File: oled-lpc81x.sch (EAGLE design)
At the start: 14 parts, among them X1 PIIKKIRIMA-2X8, X2 PIIKKIRIMA-8

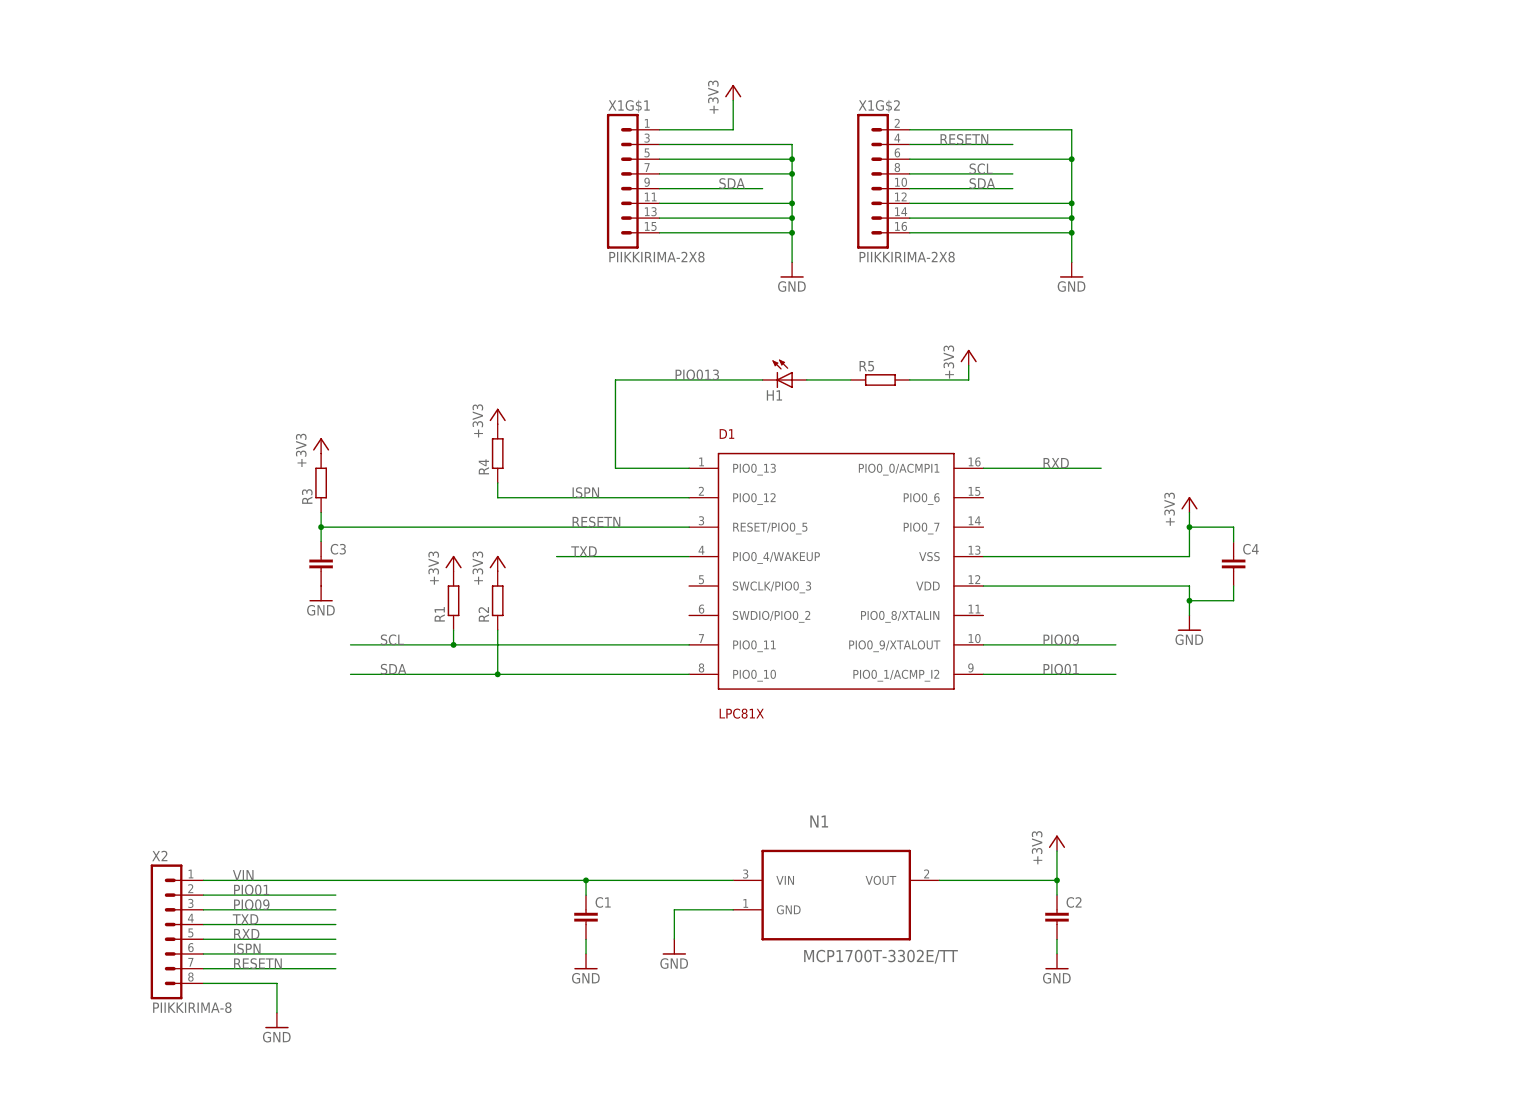
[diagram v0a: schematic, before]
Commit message: Changed busses
OLED now 3-wire SPI
I2C external to header
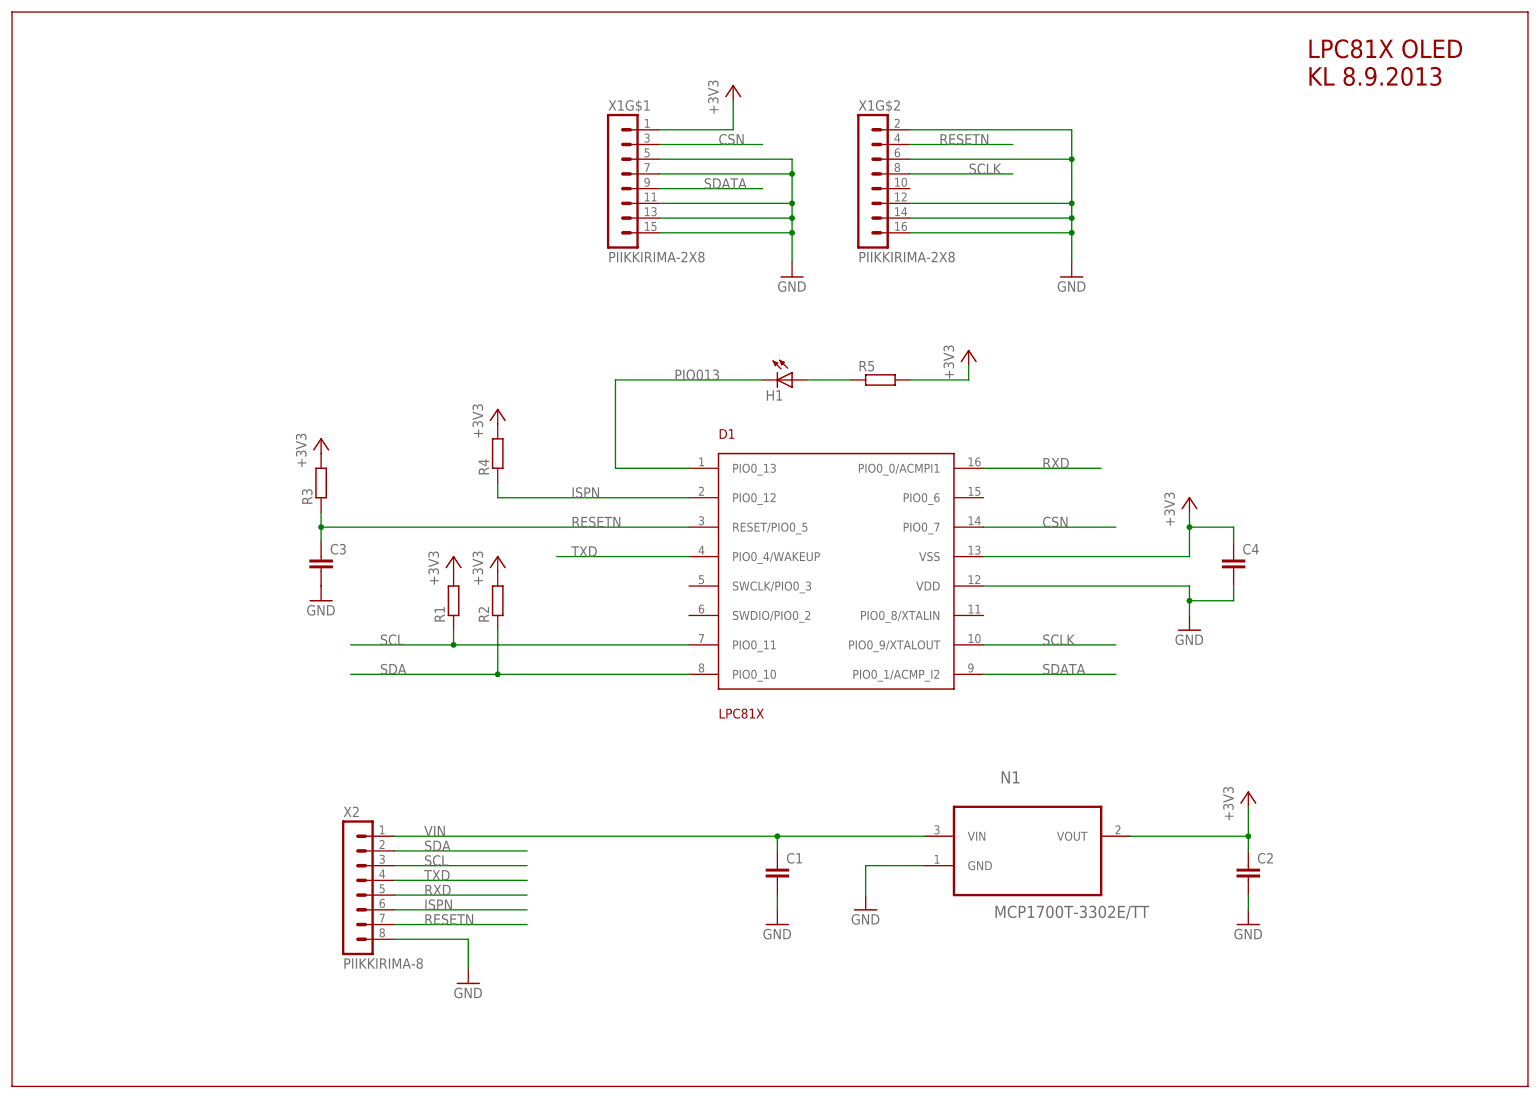
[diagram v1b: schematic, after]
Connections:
- removed net PIO01: D1.PIO0_1/ACMP_I2, X2.2
- removed net PIO09: D1.PIO0_9/XTALOUT, X2.3
- new net CSN: D1.PIO0_7, X1G$1.2
- new net SCLK: D1.PIO0_9/XTALOUT, X1G$2.4
- new net SDATA: D1.PIO0_1/ACMP_I2, X1G$1.5
- net GND: no longer X1G$1.2
- net SCL: now also X2.3; no longer X1G$2.4
- net SDA: now also X2.2; no longer X1G$2.5
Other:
- note added: "LPC81X OLED KL 8.9.2013"
- moved on the sheet: C1, C2, N1, X2

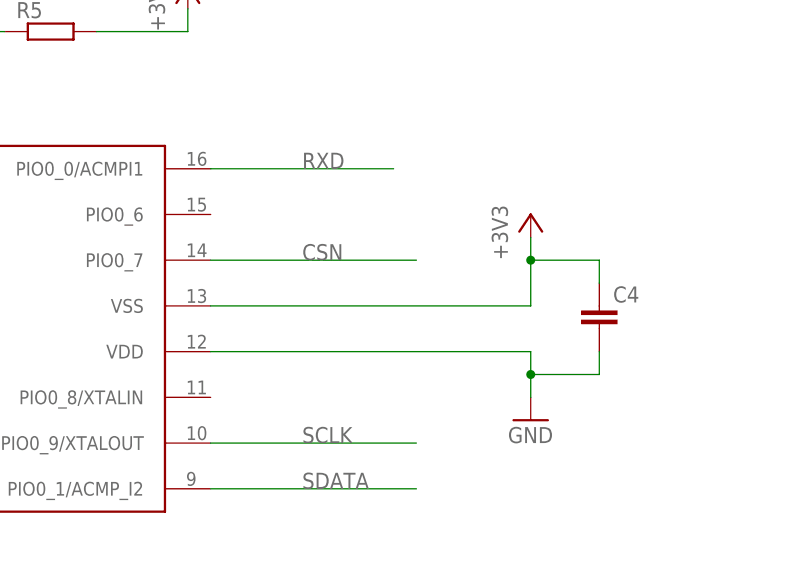
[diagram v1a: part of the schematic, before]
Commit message: v2 - VDD/VSS connection to LPC812 corrected.
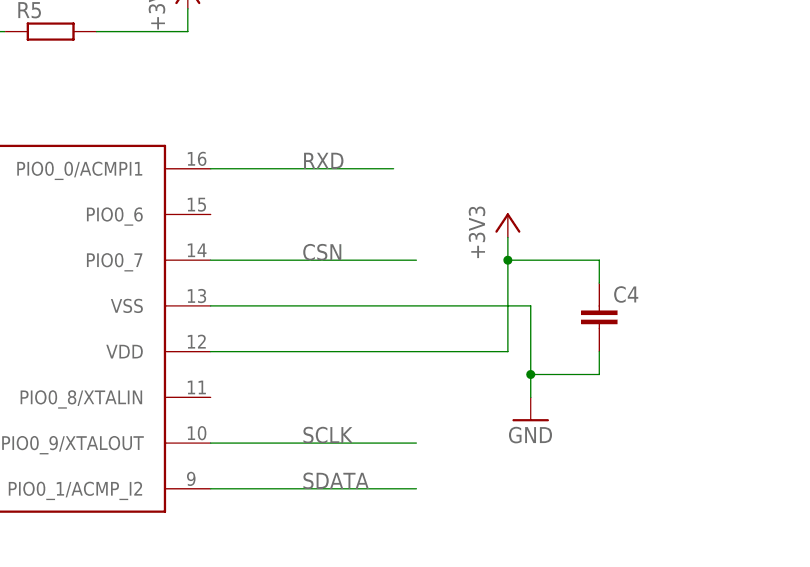
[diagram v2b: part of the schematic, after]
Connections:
- net +3V3: now also D1.VDD; no longer D1.VSS
- net GND: now also D1.VSS; no longer D1.VDD
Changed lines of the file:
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@@
 <instance part="GND5" gate="1" x="152.4" y="-76.2"/>
 <instance part="GND6" gate="1" x="142.24" y="-25.4"/>
-<instance part="+3V3" gate="G$1" x="142.24" y="-2.54"/>
+<instance part="+3V3" gate="G$1" x="139.7" y="-2.54"/>
 <instance part="C1" gate="G$1" x="71.12" y="-66.04"/>
 <instance part="C2" gate="G$1" x="152.4" y="-66.04"/>
@@
 </segment>
 <segment>
-<pinref part="D1" gate="G$1" pin="VSS"/>
-<wire x1="106.68" y1="-12.7" x2="142.24" y2="-12.7" width="0.1524" layer="91"/>
-<wire x1="142.24" y1="-12.7" x2="142.24" y2="-7.62" width="0.1524" layer="91"/>
 <pinref part="+3V3" gate="G$1" pin="+3V3"/>
 <pinref part="C4" gate="G$1" pin="1"/>
-<wire x1="142.24" y1="-7.62" x2="142.24" y2="-5.08" width="0.1524" layer="91"/>
-<wire x1="142.24" y1="-7.62" x2="149.86" y2="-7.62" width="0.1524" layer="91"/>
+<wire x1="139.7" y1="-7.62" x2="139.7" y2="-5.08" width="0.1524" layer="91"/>
+<wire x1="139.7" y1="-7.62" x2="149.86" y2="-7.62" width="0.1524" layer="91"/>
 <wire x1="149.86" y1="-7.62" x2="149.86" y2="-10.16" width="0.1524" layer="91"/>
-<junction x="142.24" y="-7.62"/>
+<junction x="139.7" y="-7.62"/>
+<pinref part="D1" gate="G$1" pin="VDD"/>
+<wire x1="106.68" y1="-17.78" x2="139.7" y2="-17.78" width="0.1524" layer="91"/>
+<wire x1="139.7" y1="-17.78" x2="139.7" y2="-7.62" width="0.1524" layer="91"/>
 </segment>
 <segment>
@@
 </segment>
 <segment>
-<pinref part="D1" gate="G$1" pin="VDD"/>
-<wire x1="106.68" y1="-17.78" x2="142.24" y2="-17.78" width="0.1524" layer="91"/>
-<wire x1="142.24" y1="-17.78" x2="142.24" y2="-20.32" width="0.1524" layer="91"/>
 <pinref part="GND6" gate="1" pin="GND"/>
 <pinref part="C4" gate="G$1" pin="2"/>
@@
 <wire x1="142.24" y1="-20.32" x2="149.86" y2="-20.32" width="0.1524" layer="91"/>
 <wire x1="149.86" y1="-20.32" x2="149.86" y2="-17.78" width="0.1524" layer="91"/>
+<wire x1="142.24" y1="-20.32" x2="142.24" y2="-12.7" width="0.1524" layer="91"/>
 <junction x="142.24" y="-20.32"/>
+<pinref part="D1" gate="G$1" pin="VSS"/>
+<wire x1="142.24" y1="-12.7" x2="106.68" y2="-12.7" width="0.1524" layer="91"/>
 </segment>
 <segment>
